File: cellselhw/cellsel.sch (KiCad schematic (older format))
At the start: 59 parts, among them P1 CONN_01X04, P2 CONN_01X04, P3 CONN_01X04, P4 CONN_01X04, P5 CONN_01X08, P6 CONN_01X08, P7 CONN_01X03, P8 CONN_01X04, Q1 ZXMP10A18G, Q2 FQT4N20L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

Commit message: PCB RC1 Ready
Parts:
- removed Q2: FQT4N20L, TO_SOT_Packages_SMD:SOT-223, symbol Q_NMOS_GDSD
- added Q2: FDV303N, TO_SOT_Packages_SMD:SOT-23, symbol Q_NMOS_GSD
- added R23, R24: 33k, Resistors_SMD:R_0603, symbol R
- P3: footprint Connectors_Molex:Molex_KK-6410-04_04x2.54mm_Straight -> Custom_Descretes:MINICON_01X04
- P7: footprint Connectors_Molex:Molex_KK-6410-03_03x2.54mm_Straight -> Custom_Descretes:DS18B20
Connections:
- net DISCH_BUSA: now also R24.2
- net DISCH_BUSB: now also R23.2
- net GND: now also C10.1, C11.1, C9.1, P3.4 (P4), U4.28 (VSS), Q2.2 (S), R23.1, R24.1
- net RS485RXEN: now also U4.5 (P1.3); no longer U4.14 (P3.3)
- net RS485TXEN: now also U4.2 (P1.0); no longer U4.13 (P3.2)
- net SW5VEN: now also U4.8 (P3.1); no longer U4.20 (P3.6)
- net SWGNDEN: now also U4.9 (P3.0); no longer U4.19 (P3.5)
- net at C11.2, R17.1, U4.24 (~RST): now also P3.2 (P2); no longer P3.3 (P3)
- net at U4.25 (TEST): now also P3.3 (P3); no longer P3.2 (P2)
- net at R10.1, R6.1: now also Q2.1 (G)
- net at Q1.1 (G), R3.1: now also Q2.3 (D)
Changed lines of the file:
@@
-$EndComp
-$Comp
-L Q_NMOS_GDSD Q2
-U 1 1 5A75DF39
-P 5500 1500
-F 0 "Q2" H 5800 1550 50  0000 R CNN
-F 1 "FQT4N20L" H 6050 1450 50  0000 R CNN
-F 2 "TO_SOT_Packages_SMD:SOT-223" H 5700 1600 50  0001 C CNN
-F 3 "" H 5500 1500 50  0000 C CNN
-	1    5500 1500
-	1    0    0    -1
 $EndComp
 $Comp
@@
 Wire Wire Line
 	5500 1200 6000 1200
-Wire Wire Line
-	5700 1200 5700 1300
 Connection ~ 5600 1200
-Connection ~ 5700 1200
 Wire Wire Line
 	6300 900  6300 1000
@@
 Text GLabel 1100 3600 0    60   Input ~ 0
 UCA0TXD
-Text GLabel 1100 4500 0    60   Input ~ 0
+Text GLabel 1100 3400 0    60   Input ~ 0
 RS485TXEN
-Text GLabel 1100 4600 0    60   Input ~ 0
+Text GLabel 1100 3700 0    60   Input ~ 0
 RS485RXEN
 Text GLabel 3100 6700 2    60   Input ~ 0
@@
 Wire Wire Line
 	1100 3600 1200 3600
-Wire Wire Line
-	1100 4500 1200 4500
-Wire Wire Line
-	1100 4600 1200 4600
 Text GLabel 6400 4500 0    60   Input ~ 0
 IOEXRST
@@
 F 0 "P3" H 3800 2900 50  0000 C CNN
 F 1 "CONN_01X04" V 3900 2650 50  0000 C CNN
-F 2 "Connectors_Molex:Molex_KK-6410-04_04x2.54mm_Straight" H 3800 2650 50  0001 C CNN
+F 2 "Custom_Descretes:MINICON_01X04" H 3800 2650 50  0001 C CNN
 F 3 "" H 3800 2650 50  0000 C CNN
 	1    3800 2650
@@
 $EndComp
 Wire Wire Line
-	3100 2700 3100 3700
+	3100 2600 3100 3700
 Wire Wire Line
 	2600 3600 3000 3600
-Wire Wire Line
-	3000 3600 3000 2600
-Wire Wire Line
-	3000 2600 3600 2600
-Wire Wire Line
-	3100 2700 3600 2700
 Wire Wire Line
 	1000 2500 3600 2500
@@
 	3400 3200 3400 2800
 Connection ~ 3400 2800
-Text GLabel 3150 4100 2    60   Input ~ 0
+Text GLabel 1100 4000 0    60   Input ~ 0
 SW5VEN
-Text GLabel 3150 4200 2    60   Input ~ 0
+Text GLabel 1100 4100 0    60   Input ~ 0
 SWGNDEN
-Wire Wire Line
-	3150 4100 2600 4100
-Wire Wire Line
-	2600 4200 3150 4200
 Connection ~ 1100 2500
 Text GLabel 5000 900  0    60   Input ~ 0
@@
 Connection ~ 7800 1800
 Wire Wire Line
-	7800 2400 7800 2300
+	7800 2300 7800 2500
 Wire Wire Line
 	5200 2400 8500 2400
 Wire Wire Line
-	7200 2400 7200 2300
+	7200 2300 7200 2500
 Connection ~ 7200 2400
 Connection ~ 7800 2400
@@
 	7300 1800 7300 1900
 Connection ~ 7200 1800
-Text GLabel 7500 2500 2    60   Input ~ 0
+Text GLabel 7950 2900 2    60   Input ~ 0
 DISCH_BUSA
-Text GLabel 6900 2700 2    60   Input ~ 0
+Text GLabel 6700 2900 0    60   Input ~ 0
 DISCH_BUSB
 Wire Wire Line
 	7500 2100 7400 2100
 Wire Wire Line
-	7400 2100 7400 2500
-Wire Wire Line
-	7400 2500 7500 2500
-Wire Wire Line
-	6900 2700 6800 2700
-Wire Wire Line
-	6800 2700 6800 2100
+	6800 2100 6800 2900
 Wire Wire Line
 	6800 2100 6900 2100
@@
 F 0 "P7" H 2400 5600 50  0000 C CNN
 F 1 "CONN_01X03" V 2500 5400 50  0000 C CNN
-F 2 "Connectors_Molex:Molex_KK-6410-03_03x2.54mm_Straight" H 2400 5400 50  0001 C CNN
+F 2 "Custom_Descretes:DS18B20" H 2400 5400 50  0001 C CNN
 F 3 "" H 2400 5400 50  0000 C CNN
 	1    2400 5400
@@
 Text Notes 4350 6400 0    60   ~ 0
 ULN2803A Inputs will float (because MCP23017 is in reset mode)\nuntil the MSP430G2553 has initialised. The ULN2803A has internal\npull-down resistors so this short-lived condition is ok.
+Wire Wire Line
+	6700 2900 7200 2900
+$Comp
+L R R23
+U 1 1 5AA3F5FA
+P 7200 2650
+F 0 "R23" V 7280 2650 50  0000 C CNN
+F 1 "33k" V 7200 2650 50  0000 C CNN
+F 2 "Resistors_SMD:R_0603" V 7130 2650 50  0001 C CNN
+F 3 "" H 7200 2650 50  0000 C CNN
+	1    7200 2650
+	1    0    0    -1
+$EndComp
+$Comp
+L R R24
+U 1 1 5AA3F6C7
+P 7800 2650
+F 0 "R24" V 7880 2650 50  0000 C CNN
+F 1 "33k" V 7800 2650 50  0000 C CNN
+F 2 "Resistors_SMD:R_0603" V 7730 2650 50  0001 C CNN
+F 3 "" H 7800 2650 50  0000 C CNN
+	1    7800 2650
+	1    0    0    -1
+$EndComp
+Wire Wire Line
+	7400 2100 7400 2900
+Wire Wire Line
+	7400 2900 7950 2900
+Wire Wire Line
+	7800 2800 7800 2900
+Connection ~ 7800 2900
+Wire Wire Line
+	7200 2900 7200 2800
+Connection ~ 6800 2900
+Wire Wire Line
+	1100 4000 1200 4000
+Wire Wire Line
+	1100 4100 1200 4100
+Wire Wire Line
+	1100 3700 1200 3700
+Wire Wire Line
+	1100 3400 1200 3400
+Wire Wire Line
+	3100 2600 3600 2600
+Wire Wire Line
+	3600 2700 3000 2700
+Wire Wire Line
+	3000 2700 3000 3600
+$Comp
+L Q_NMOS_GSD Q2
+U 1 1 5AA418B4
+P 5500 1500
+F 0 "Q2" H 5800 1550 50  0000 R CNN
+F 1 "FDV303N" H 6000 1450 50  0000 R CNN
+F 2 "TO_SOT_Packages_SMD:SOT-23" H 5700 1600 50  0001 C CNN
+F 3 "" H 5500 1500 50  0000 C CNN
+	1    5500 1500
+	1    0    0    -1
+$EndComp
+$Comp
+L GND #PWR?
+U 1 1 5AA42C4C
+P 2800 3100
+F 0 "#PWR?" H 2800 2850 50  0001 C CNN
+F 1 "GND" H 2800 2950 50  0000 C CNN
+F 2 "" H 2800 3100 50  0000 C CNN
+F 3 "" H 2800 3100 50  0000 C CNN
+	1    2800 3100
+	1    0    0    -1
+$EndComp
+Wire Wire Line
+	2700 3000 2800 3000
+Wire Wire Line
+	2800 3000 2800 3100
+Connection ~ 2700 3000
 $EndSCHEMATC

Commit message: Final Production Ready Prototype
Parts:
- added P9: CONN_01X04, Connectors_Molex:Molex_KK-6410-04_04x2.54mm_Straight, symbol CONN_01X04
- R21, R22: value 10k -> 33k
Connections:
- net 3V3: now also P9.1 (P1)
- net GND: now also P9.4 (P4)

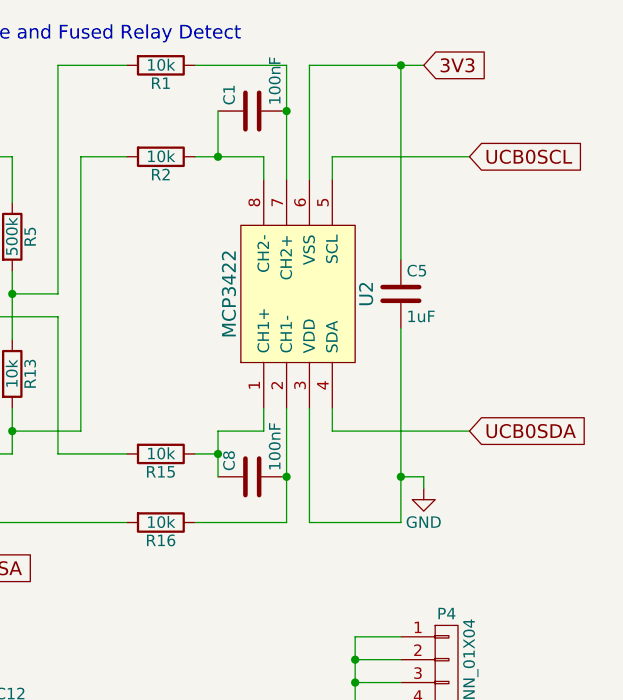
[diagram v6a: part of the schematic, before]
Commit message: Connected Power Incorrectly on ADC
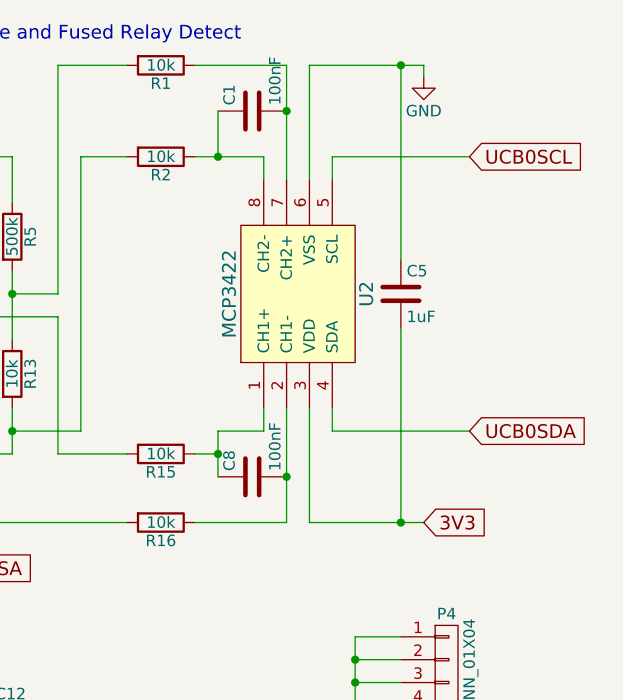
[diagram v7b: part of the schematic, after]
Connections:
- net 3V3: now also C5.2, U2.3 (VDD); no longer C5.1, U2.6 (VSS)
- net GND: now also C5.1, U2.6 (VSS); no longer C5.2, U2.3 (VDD)
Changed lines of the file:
@@
 LIBS:contrib
 LIBS:valves
-LIBS:vreg
 LIBS:msp430
-LIBS:powerswitchics
-LIBS:ioexpanders
-LIBS:adcanddac
-LIBS:ti
-LIBS:transientsuppressor
 LIBS:cellsel-cache
 EELAYER 25 0
@@
 12V
 $Comp
-L GND #PWR7
+L GND #PWR01
 U 1 1 5A764632
 P 7600 6100
-F 0 "#PWR7" H 7600 5850 50  0001 C CNN
+F 0 "#PWR01" H 7600 5850 50  0001 C CNN
 F 1 "GND" H 7600 5950 50  0000 C CNN
 F 2 "" H 7600 6100 50  0000 C CNN
@@
 12V
 $Comp
-L GND #PWR2
+L GND #PWR02
 U 1 1 5A77F477
 P 1700 2300
-F 0 "#PWR2" H 1700 2050 50  0001 C CNN
+F 0 "#PWR02" H 1700 2050 50  0001 C CNN
 F 1 "GND" H 1700 2150 50  0000 C CNN
 F 2 "" H 1700 2300 50  0000 C CNN
@@
 $EndComp
 $Comp
-L GND #PWR1
+L GND #PWR03
 U 1 1 5A77F4F1
 P 1700 1400
-F 0 "#PWR1" H 1700 1150 50  0001 C CNN
+F 0 "#PWR03" H 1700 1150 50  0001 C CNN
 F 1 "GND" H 1700 1250 50  0000 C CNN
 F 2 "" H 1700 1400 50  0000 C CNN
@@
 $EndComp
 $Comp
-L GND #PWR6
+L GND #PWR04
 U 1 1 5A781864
 P 6450 2500
-F 0 "#PWR6" H 6450 2250 50  0001 C CNN
+F 0 "#PWR04" H 6450 2250 50  0001 C CNN
 F 1 "GND" H 6450 2350 50  0000 C CNN
 F 2 "" H 6450 2500 50  0000 C CNN
@@
 	1    0    0    -1
 $EndComp
-Text GLabel 10300 700  2    60   Input ~ 0
+Text GLabel 10300 2700 2    60   Input ~ 0
 3V3
 $Comp
-L GND #PWR8
+L GND #PWR05
 U 1 1 5A782C52
-P 10300 2550
-F 0 "#PWR8" H 10300 2300 50  0001 C CNN
-F 1 "GND" H 10300 2400 50  0000 C CNN
-F 2 "" H 10300 2550 50  0000 C CNN
-F 3 "" H 10300 2550 50  0000 C CNN
-	1    10300 2550
+P 10300 750
+F 0 "#PWR05" H 10300 500 50  0001 C CNN
+F 1 "GND" H 10300 600 50  0000 C CNN
+F 2 "" H 10300 750 50  0000 C CNN
+F 3 "" H 10300 750 50  0000 C CNN
+	1    10300 750
 	1    0    0    -1
 $EndComp
@@
 3V3
 $Comp
-L GND #PWR5
+L GND #PWR06
 U 1 1 5A7872C8
 P 3600 6200
-F 0 "#PWR5" H 3600 5950 50  0001 C CNN
+F 0 "#PWR06" H 3600 5950 50  0001 C CNN
 F 1 "GND" H 3600 6050 50  0000 C CNN
 F 2 "" H 3600 6200 50  0000 C CNN
@@
 3V3
 $Comp
-L GND #PWR3
+L GND #PWR07
 U 1 1 5A7F06B7
 P 2700 5600
-F 0 "#PWR3" H 2700 5350 50  0001 C CNN
+F 0 "#PWR07" H 2700 5350 50  0001 C CNN
 F 1 "GND" H 2700 5450 50  0000 C CNN
 F 2 "" H 2700 5600 50  0000 C CNN
@@
 $EndComp
 $Comp
-L GND #PWR4
+L GND #PWR08
 U 1 1 5AA42C4C
 P 2800 3100
-F 0 "#PWR4" H 2800 2850 50  0001 C CNN
+F 0 "#PWR08" H 2800 2850 50  0001 C CNN
 F 1 "GND" H 2800 2950 50  0000 C CNN
 F 2 "" H 2800 3100 50  0000 C CNN
@@
 	9800 2200 9800 2700
 Wire Wire Line
-	9800 2700 10200 2700
-Wire Wire Line
-	10200 2700 10200 1850
+	9800 2700 10300 2700
 Wire Wire Line
 	9900 1200 9900 1100
@@
 Connection ~ 5100 900
 Wire Wire Line
-	10300 2550 10300 2500
-Wire Wire Line
-	10300 2500 10200 2500
-Connection ~ 10200 2500
-Wire Wire Line
-	9800 700  10300 700
-Connection ~ 10200 700
-Wire Wire Line
 	8400 3300 8400 3400
 Wire Wire Line
@@
 	9400 2300 9600 2300
 Connection ~ 9400 2400
-Wire Wire Line
-	9800 1200 9800 700
-Wire Wire Line
-	10200 700  10200 1550
 Wire Wire Line
 	3150 4300 2600 4300
@@
 Connection ~ 3600 2500
 Connection ~ 3600 2800
+Wire Wire Line
+	10300 750  10300 700
+Wire Wire Line
+	10300 700  9800 700
+Wire Wire Line
+	9800 700  9800 1200
+Wire Wire Line
+	10200 1550 10200 700
+Connection ~ 10200 700
+Wire Wire Line
+	10200 2700 10200 1850
+Connection ~ 10200 2700
 $EndSCHEMATC
